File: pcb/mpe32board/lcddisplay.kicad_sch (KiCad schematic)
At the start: 3 parts, among them J45 Conn_01x04_Socket

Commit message: layout stuff
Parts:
- J45: footprint (none) -> Connector_PinHeader_2.54mm:PinHeader_1x04_P2.54mm_Vertical
- R21, R22: footprint (none) -> Resistor_SMD:R_0603_1608Metric
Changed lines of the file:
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@@
 			)
 		)
-		(property "Footprint" ""
+		(property "Footprint" "Connector_PinHeader_2.54mm:PinHeader_1x04_P2.54mm_Vertical"
 			(at 144.78 85.09 0)
 			(effects
@@
 			)
 		)
-		(property "Footprint" ""
+		(property "Footprint" "Resistor_SMD:R_0603_1608Metric"
 			(at 184.15 87.63 0)
 			(effects
@@
 			)
 		)
-		(property "Footprint" ""
+		(property "Footprint" "Resistor_SMD:R_0603_1608Metric"
 			(at 184.15 82.55 0)
 			(effects

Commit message: routed ram
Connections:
- net I2C1_SCL renamed I2C4_SCL
- net I2C1_SDA renamed I2C4_SDA
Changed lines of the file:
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@@
 		)
 	)
-	(global_label "I2C1_SCL"
-		(shape input)
-		(at 181.61 82.55 180)
-		(fields_autoplaced yes)
-		(effects
-			(font
-				(size 1.27 1.27)
-			)
-			(justify right)
-		)
-		(property "Intersheetrefs" "${INTERSHEET_REFS}"
-			(at 169.8558 82.55 0)
-			(hide yes)
-			(show_name no)
-			(do_not_autoplace no)
-			(effects
-				(font
-					(size 1.27 1.27)
-				)
-				(justify right)
-			)
-		)
-	)
-	(global_label "I2C1_SDA"
+	(global_label "I2C4_SDA"
 		(shape input)
 		(at 181.61 87.63 180)
@@
 		)
 	)
-	(global_label "I2C1_SDA"
+	(global_label "I2C4_SDA"
 		(shape input)
 		(at 139.7 85.09 180)
@@
 		)
 	)
-	(global_label "I2C1_SCL"
+	(global_label "I2C4_SCL"
 		(shape input)
 		(at 139.7 82.55 180)
@@
 			(hide yes)
 			(show_name no)
+			(do_not_autoplace no)
+			(effects
+				(font
+					(size 1.27 1.27)
+				)
+				(justify right)
+			)
+		)
+	)
+	(global_label "I2C4_SCL"
+		(shape input)
+		(at 181.61 82.55 180)
+		(fields_autoplaced yes)
+		(effects
+			(font
+				(size 1.27 1.27)
+			)
+			(justify right)
+		)
+		(property "Intersheetrefs" "${INTERSHEET_REFS}"
+			(at 169.8558 82.55 0)
+			(hide yes)
+			(show_name no)

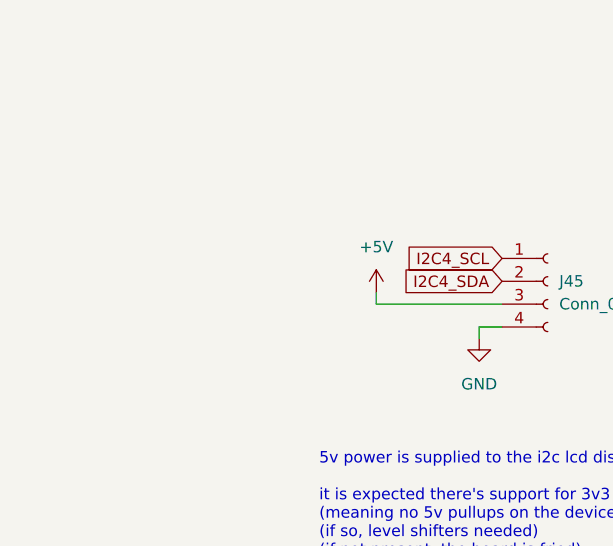
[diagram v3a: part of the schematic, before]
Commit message: routed audio codec and sdram
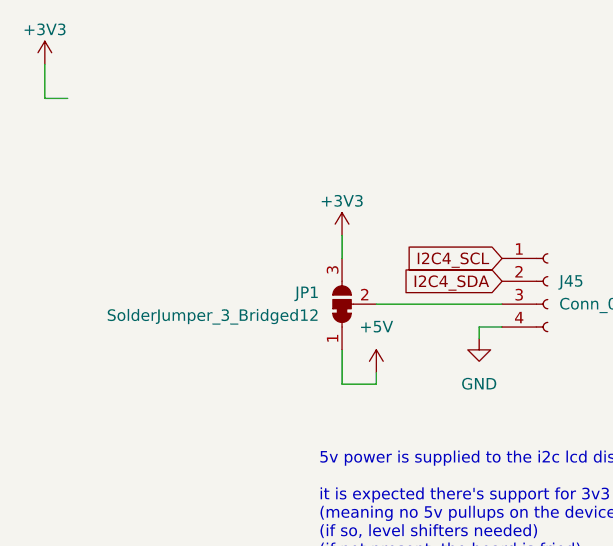
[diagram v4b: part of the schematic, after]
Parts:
- added JP1: SolderJumper_3_Bridged12, Jumper:SolderJumper-3_P1.3mm_Bridged12_RoundedPad1.0x1.5mm, symbol Jumper:SolderJumper_3_Bridged12
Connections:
- net +3V3: now also JP1.3 (B)
- net +5V: now also JP1.1 (A); no longer J45.3 (Pin_3)
- new net: J45.3 (Pin_3), JP1.2 (C)

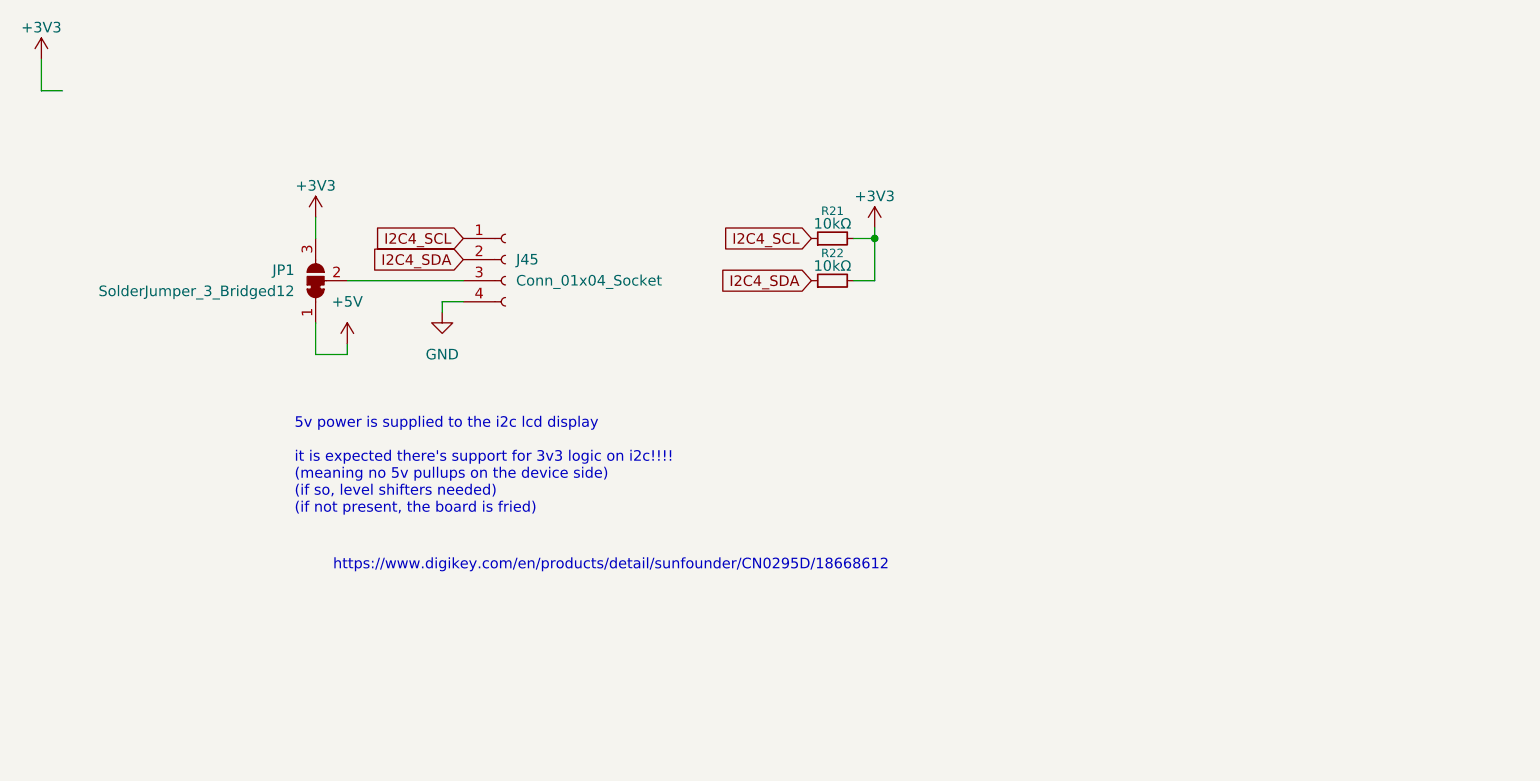
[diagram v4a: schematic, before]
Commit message: add lcd level shifter, lm1117 ldo
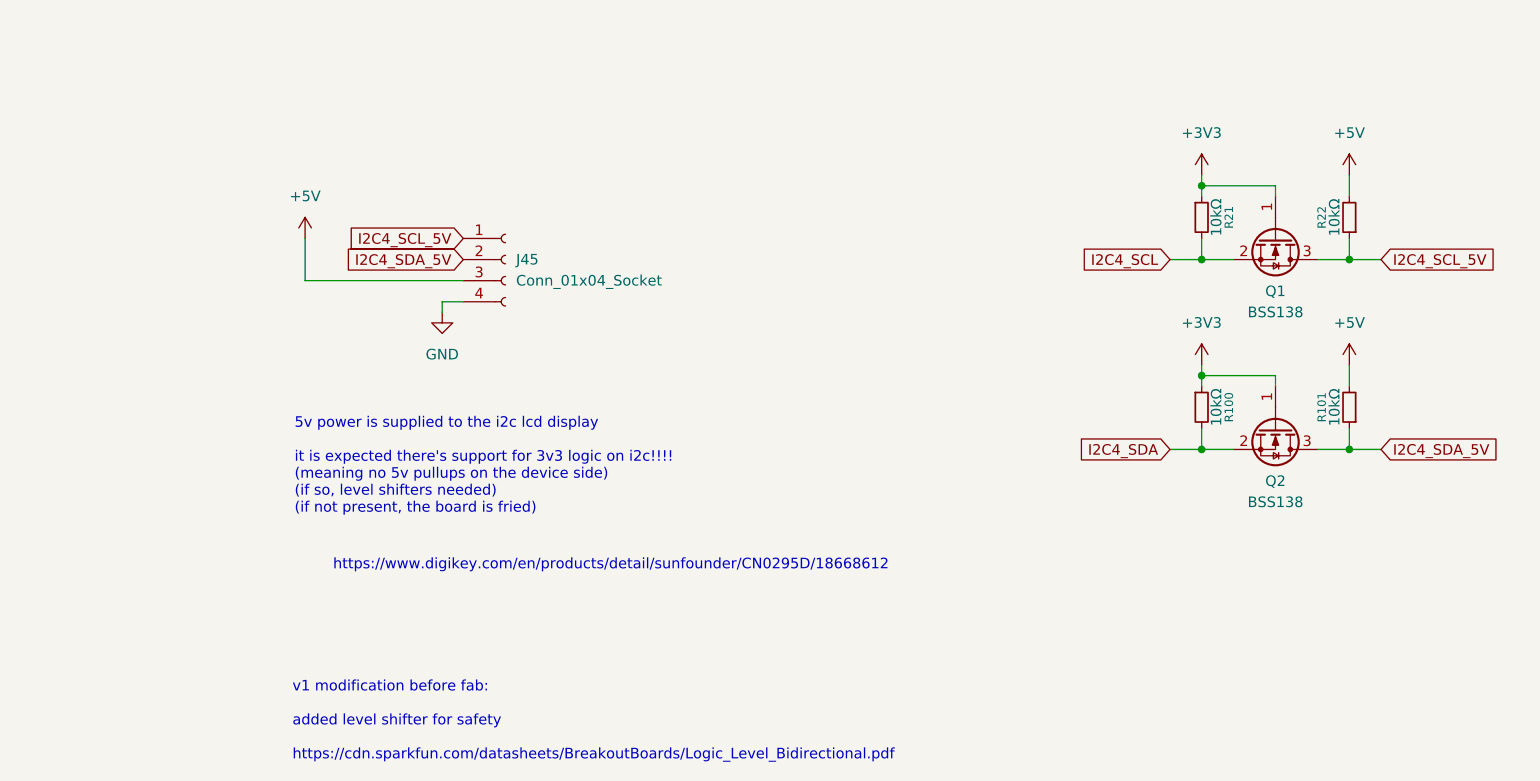
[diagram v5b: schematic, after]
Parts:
- removed JP1: SolderJumper_3_Bridged12, Jumper:SolderJumper-3_P1.3mm_Bridged12_RoundedPad1.0x1.5mm, symbol Jumper:SolderJumper_3_Bridged12
- added Q1, Q2: BSS138, Package_TO_SOT_SMD:SOT-23, symbol Transistor_FET:BSS138
- added R100, R101: 10kΩ, Resistor_SMD:R_0603_1608Metric, symbol Device:R_Small
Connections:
- net +3V3: now also R21.1, Q1.1 (G), Q2.1 (G), R100.1; no longer R21.2, R22.2
- net +5V: now also J45.3 (Pin_3), R22.2, R101.2
- net I2C4_SCL: now also R21.2, Q1.2 (S); no longer J45.1 (Pin_1), R21.1
- net I2C4_SDA: now also Q2.2 (S), R100.2; no longer J45.2 (Pin_2), R22.1
- new net I2C4_SCL_5V: J45.1 (Pin_1), Q1.3 (D), R22.1
- new net I2C4_SDA_5V: J45.2 (Pin_2), Q2.3 (D), R101.1
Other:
- note added: "v1 modification before fab: added level shifter for safety https://cdn.sparkfun.com/datasheets/BreakoutBoards/Logic_Level_Bidirectional.pdf"
